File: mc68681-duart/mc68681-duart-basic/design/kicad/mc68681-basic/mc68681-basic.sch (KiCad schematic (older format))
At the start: 34 parts, among them IC1 XR68C681CJTR-F, IC2 74HCT245, IC3 74HCT245, IC4 74HCT245, IC5 74125, IC6 IC6_DECO.PLD, IC7 IC7_UART_.PLD, J1 Conn_02x32_Odd_Even, J2 EXTBUS, J3 UART_A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

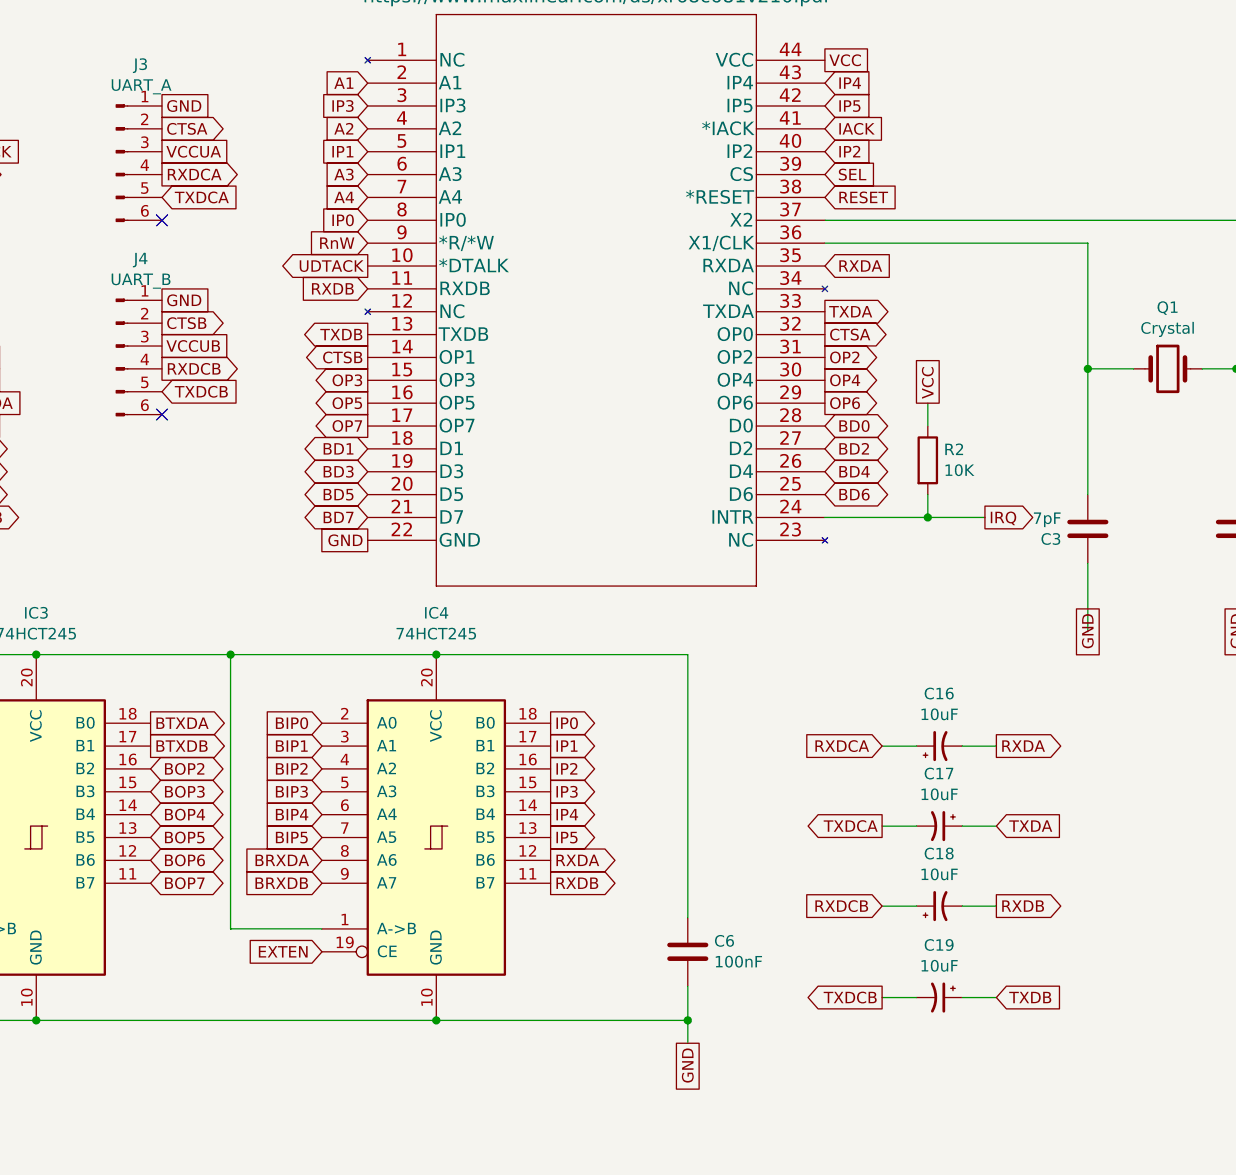
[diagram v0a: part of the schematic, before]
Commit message: Revert "DUART 2.1"
This reverts commit 27795c8f7bdad45632c07cace90e5a666905ce82.
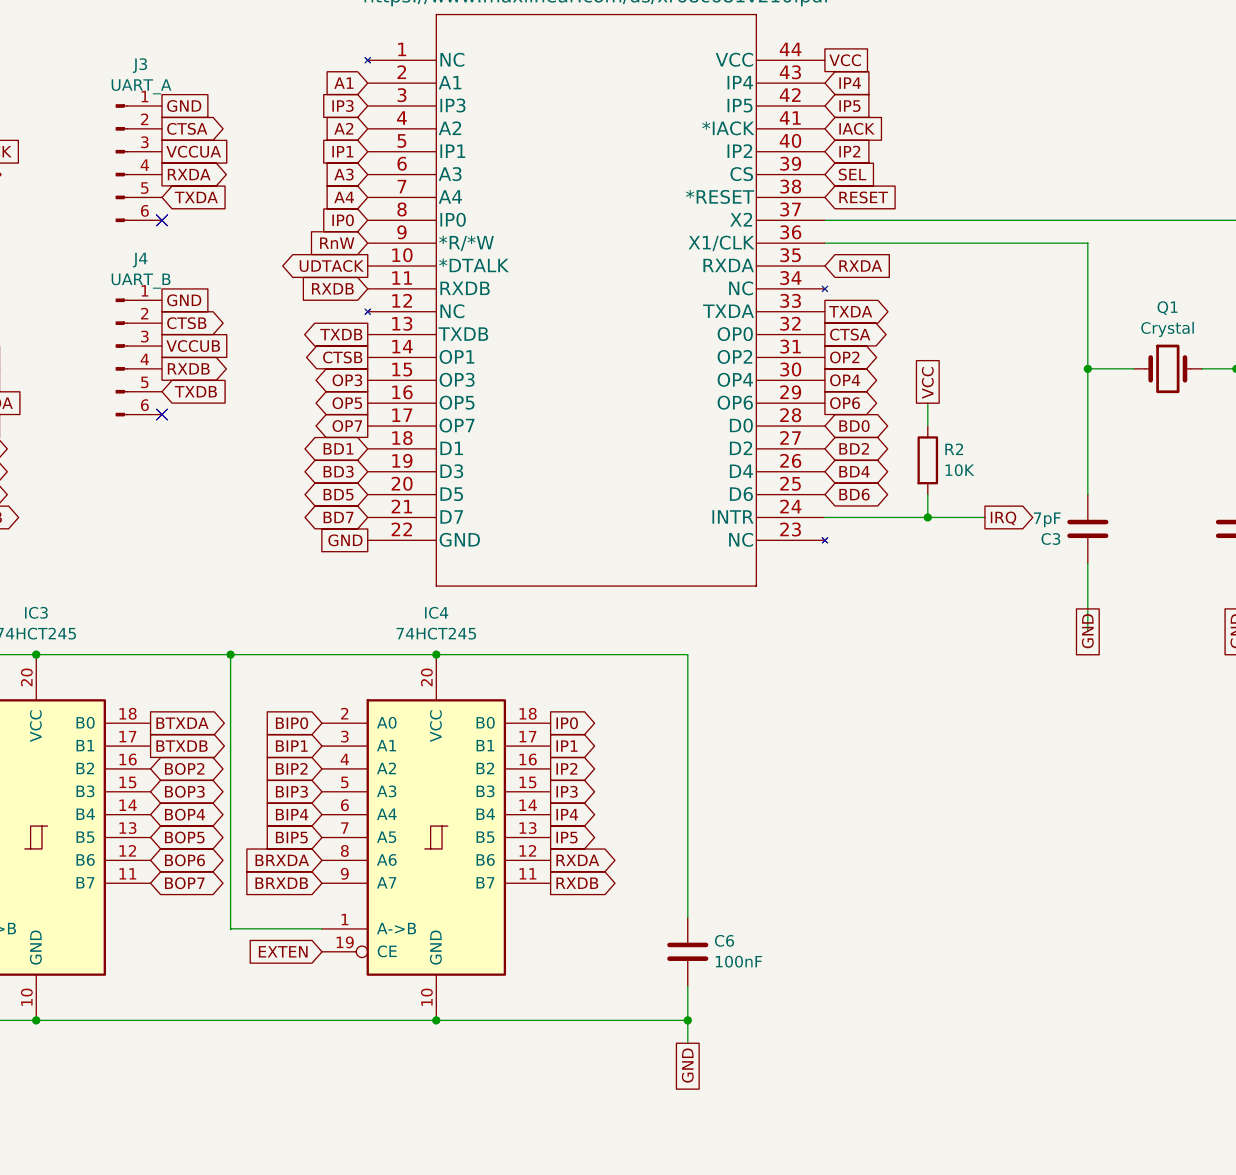
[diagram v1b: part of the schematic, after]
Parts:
- removed C16, C17, C18, C19: 10uF, Capacitor_THT:CP_Radial_D5.0mm_P2.00mm, symbol Device:CP1_Small
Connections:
- net RXDCA is gone; now on net RXDA: J3.4 (Pin_4)
- net RXDCB is gone; now on net RXDB: J4.4 (Pin_4)
- net TXDCA is gone; now on net TXDA: J3.5 (Pin_5)
- net TXDCB is gone; now on net TXDB: J4.5 (Pin_5)
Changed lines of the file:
@@
 Sheet 1 1
 Title "ROSCO_M68K MC68681 DUART EXPANSION"
-Date "2021-06-26"
-Rev "2.1"
+Date "2021-03-01"
+Rev "2"
 Comp "The Really Old School Company Limited"
 Comment1 ""
@@
 CTSA
 Text GLabel 2500 3700 2    50   Input ~ 0
-TXDCA
+TXDA
 Text GLabel 2500 3600 2    50   Output ~ 0
-RXDCA
+RXDA
 NoConn ~ 2500 3800
 Text GLabel 10550 5350 2    50   UnSpc ~ 0
@@
 CTSB
 Text GLabel 2500 4550 2    50   Input ~ 0
-TXDCB
+TXDB
 Text GLabel 2500 4450 2    50   Output ~ 0
-RXDCB
+RXDB
 NoConn ~ 2500 4650
 $Comp
@@
 Wire Wire Line
 	8750 5250 9550 5250
-Text GLabel 5650 6100 0    50   Input ~ 0
-RXDCA
-$Comp
-L Device:CP1_Small C16
-U 1 1 60D6C450
-P 5900 6100
-F 0 "C16" V 6128 6100 50  0000 C CNN
-F 1 "10uF" V 6037 6100 50  0000 C CNN
-F 2 "Capacitor_THT:CP_Radial_D5.0mm_P2.00mm" H 5900 6100 50  0001 C CNN
-F 3 "~" H 5900 6100 50  0001 C CNN
-	1    5900 6100
-	0    -1   -1   0
-$EndComp
-$Comp
-L Device:CP1_Small C17
-U 1 1 60D6DFF3
-P 5900 6450
-F 0 "C17" V 5672 6450 50  0000 C CNN
-F 1 "10uF" V 5763 6450 50  0000 C CNN
-F 2 "Capacitor_THT:CP_Radial_D5.0mm_P2.00mm" H 5900 6450 50  0001 C CNN
-F 3 "~" H 5900 6450 50  0001 C CNN
-	1    5900 6450
-	0    1    1    0
-$EndComp
-$Comp
-L Device:CP1_Small C18
-U 1 1 60D73E6D
-P 5900 6800
-F 0 "C18" V 6128 6800 50  0000 C CNN
-F 1 "10uF" V 6037 6800 50  0000 C CNN
-F 2 "Capacitor_THT:CP_Radial_D5.0mm_P2.00mm" H 5900 6800 50  0001 C CNN
-F 3 "~" H 5900 6800 50  0001 C CNN
-	1    5900 6800
-	0    -1   -1   0
-$EndComp
-$Comp
-L Device:CP1_Small C19
-U 1 1 60D797B1
-P 5900 7200
-F 0 "C19" V 5672 7200 50  0000 C CNN
-F 1 "10uF" V 5763 7200 50  0000 C CNN
-F 2 "Capacitor_THT:CP_Radial_D5.0mm_P2.00mm" H 5900 7200 50  0001 C CNN
-F 3 "~" H 5900 7200 50  0001 C CNN
-	1    5900 7200
-	0    1    1    0
-$EndComp
-Text GLabel 5650 6800 0    50   Input ~ 0
-RXDCB
-Text GLabel 6150 6450 2    50   Input ~ 0
-TXDA
-Text GLabel 6150 7200 2    50   Input ~ 0
-TXDB
-Text GLabel 6150 6100 2    50   Output ~ 0
-RXDA
-Text GLabel 6150 6800 2    50   Output ~ 0
-RXDB
-Text GLabel 5650 6450 0    50   Output ~ 0
-TXDCA
-Text GLabel 5650 7200 0    50   Output ~ 0
-TXDCB
-Wire Wire Line
-	5650 6100 5800 6100
-Wire Wire Line
-	6000 6100 6150 6100
-Wire Wire Line
-	5650 6450 5800 6450
-Wire Wire Line
-	6000 6450 6150 6450
-Wire Wire Line
-	5650 6800 5800 6800
-Wire Wire Line
-	6000 6800 6150 6800
-Wire Wire Line
-	5650 7200 5800 7200
-Wire Wire Line
-	6000 7200 6150 7200
 $EndSCHEMATC

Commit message: DUART 2.1
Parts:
- added C16, C17, C18, C19: 10uF, Capacitor_THT:CP_Radial_D5.0mm_P2.00mm, symbol Device:CP1_Small
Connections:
- net RXDA: now also C16.2; no longer J3.4 (Pin_4)
- net RXDB: now also C18.2; no longer J4.4 (Pin_4)
- net TXDA: now also C17.1; no longer J3.5 (Pin_5)
- net TXDB: now also C19.1; no longer J4.5 (Pin_5)
- new net RXDCA: C16.1, J3.4 (Pin_4)
- new net RXDCB: C18.1, J4.4 (Pin_4)
- new net TXDCA: C17.2, J3.5 (Pin_5)
- new net TXDCB: C19.2, J4.5 (Pin_5)
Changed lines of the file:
@@
 Sheet 1 1
 Title "ROSCO_M68K MC68681 DUART EXPANSION"
-Date "2021-03-01"
-Rev "2"
+Date "2021-06-26"
+Rev "2.1"
 Comp "The Really Old School Company Limited"
 Comment1 ""
@@
 CTSA
 Text GLabel 2500 3700 2    50   Input ~ 0
-TXDA
+TXDCA
 Text GLabel 2500 3600 2    50   Output ~ 0
-RXDA
+RXDCA
 NoConn ~ 2500 3800
 Text GLabel 10550 5350 2    50   UnSpc ~ 0
@@
 CTSB
 Text GLabel 2500 4550 2    50   Input ~ 0
-TXDB
+TXDCB
 Text GLabel 2500 4450 2    50   Output ~ 0
-RXDB
+RXDCB
 NoConn ~ 2500 4650
 $Comp
@@
 Wire Wire Line
 	8750 5250 9550 5250
+Text GLabel 5650 6100 0    50   Input ~ 0
+RXDCA
+$Comp
+L Device:CP1_Small C16
+U 1 1 60D6C450
+P 5900 6100
+F 0 "C16" V 6128 6100 50  0000 C CNN
+F 1 "10uF" V 6037 6100 50  0000 C CNN
+F 2 "Capacitor_THT:CP_Radial_D5.0mm_P2.00mm" H 5900 6100 50  0001 C CNN
+F 3 "~" H 5900 6100 50  0001 C CNN
+	1    5900 6100
+	0    -1   -1   0
+$EndComp
+$Comp
+L Device:CP1_Small C17
+U 1 1 60D6DFF3
+P 5900 6450
+F 0 "C17" V 5672 6450 50  0000 C CNN
+F 1 "10uF" V 5763 6450 50  0000 C CNN
+F 2 "Capacitor_THT:CP_Radial_D5.0mm_P2.00mm" H 5900 6450 50  0001 C CNN
+F 3 "~" H 5900 6450 50  0001 C CNN
+	1    5900 6450
+	0    1    1    0
+$EndComp
+$Comp
+L Device:CP1_Small C18
+U 1 1 60D73E6D
+P 5900 6800
+F 0 "C18" V 6128 6800 50  0000 C CNN
+F 1 "10uF" V 6037 6800 50  0000 C CNN
+F 2 "Capacitor_THT:CP_Radial_D5.0mm_P2.00mm" H 5900 6800 50  0001 C CNN
+F 3 "~" H 5900 6800 50  0001 C CNN
+	1    5900 6800
+	0    -1   -1   0
+$EndComp
+$Comp
+L Device:CP1_Small C19
+U 1 1 60D797B1
+P 5900 7200
+F 0 "C19" V 5672 7200 50  0000 C CNN
+F 1 "10uF" V 5763 7200 50  0000 C CNN
+F 2 "Capacitor_THT:CP_Radial_D5.0mm_P2.00mm" H 5900 7200 50  0001 C CNN
+F 3 "~" H 5900 7200 50  0001 C CNN
+	1    5900 7200
+	0    1    1    0
+$EndComp
+Text GLabel 5650 6800 0    50   Input ~ 0
+RXDCB
+Text GLabel 6150 6450 2    50   Input ~ 0
+TXDA
+Text GLabel 6150 7200 2    50   Input ~ 0
+TXDB
+Text GLabel 6150 6100 2    50   Output ~ 0
+RXDA
+Text GLabel 6150 6800 2    50   Output ~ 0
+RXDB
+Text GLabel 5650 6450 0    50   Output ~ 0
+TXDCA
+Text GLabel 5650 7200 0    50   Output ~ 0
+TXDCB
+Wire Wire Line
+	5650 6100 5800 6100
+Wire Wire Line
+	6000 6100 6150 6100
+Wire Wire Line
+	5650 6450 5800 6450
+Wire Wire Line
+	6000 6450 6150 6450
+Wire Wire Line
+	5650 6800 5800 6800
+Wire Wire Line
+	6000 6800 6150 6800
+Wire Wire Line
+	5650 7200 5800 7200
+Wire Wire Line
+	6000 7200 6150 7200
 $EndSCHEMATC
